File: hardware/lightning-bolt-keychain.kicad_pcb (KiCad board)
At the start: 2 copper layers, 70 x 114 mm, 9 parts, among them SW1 SPST

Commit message: Repair KiCad PCB and update parts notes
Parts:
- BT1: value CR2032 -> CR1220/CR1225
- SW1: footprint Button_Switch_SMD:SW_SPST_EVQP2 -> Button_Switch_SMD:SW_SPST_EVQP2_ShortPushTravel_H2.1mm
- moved D1 18.4 mm to (88.0, 52.0)
- moved R1 18.4 mm to (88.0, 58.0)
- moved D3 16.1 mm to (78.0, 92.0)
- moved R3 16.1 mm to (78.0, 98.0)
- moved SW1 6.00 mm to (80.0, 106.0)
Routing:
- net GND: track 54.8 -> 130.0 mm, vias 2 -> 1
- net +BATT: track 18.6 -> 55.4 mm
- net VLED: track 81.4 -> 65.4 mm
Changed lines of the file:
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@@
     (rev "A")
     (company "Open hardware concept")
-    (comment 1 "CR2032 amber LED keychain")
+    (comment 1 "12mm coin-cell amber LED keychain")
   )
   (layers
@@
   (footprint "Battery:BatteryHolder_Keystone_3000_1x12mm" (layer "B.Cu")
     (at 79 80 180)
-    (descr "CR2032 holder placeholder - verify exact ordered part")
+    (descr "12 mm coin-cell retainer - Keystone 3000 style")
     (property "Sheetfile" "lightning-bolt-keychain.kicad_sch")
     (property "Sheetname" "")
@@
       (effects (font (size 1 1) (thickness 0.15)) (justify mirror))
     )
-    (property "Value" "CR2032" (at 0 -13 180) (layer "B.Fab")
+    (property "Value" "CR1220/CR1225" (at 0 -13 180) (layer "B.Fab")
       (effects (font (size 1 1) (thickness 0.15)) (justify mirror))
     )
     (attr smd)
     (fp_circle (center 0 0) (end 11 0) (stroke (width 0.15) (type solid)) (fill none) (layer "B.SilkS"))
-    (pad "1" smd roundrect (at 0 -8 180) (size 5 3) (layers "B.Cu" "B.Paste" "B.Mask") (roundrect_rratio 0.2)
+    (pad "1" smd rect (at -7.9 0 180) (size 3.5 3.3) (layers "B.Cu" "B.Paste" "B.Mask")
       (net 2 "+BATT") (pinfunction "+") (pintype "passive"))
-    (pad "2" smd circle (at 0 0 180) (size 16 16) (layers "B.Cu" "B.Mask")
+    (pad "1" smd rect (at 7.9 0 180) (size 3.5 3.3) (layers "B.Cu" "B.Paste" "B.Mask")
+      (net 2 "+BATT") (pinfunction "+") (pintype "passive"))
+    (pad "2" smd circle (at 0 0 180) (size 10.2 10.2) (layers "B.Cu" "B.Mask")
       (net 1 "GND") (pinfunction "-") (pintype "passive"))
   )
-  (footprint "Button_Switch_SMD:SW_SPST_EVQP2" (layer "B.Cu")
-    (at 86 106 0)
+  (footprint "Button_Switch_SMD:SW_SPST_EVQP2_ShortPushTravel_H2.1mm" (layer "B.Cu")
+    (at 80 106 0)
     (property "Sheetfile" "lightning-bolt-keychain.kicad_sch")
     (property "Sheetname" "")
@@
   )
   (footprint "Resistor_SMD:R_0603_1608Metric" (layer "F.Cu")
-    (at 72 49 90)
+    (at 88 58 90)
     (property "Reference" "R1" (at -2 0 180) (layer "F.SilkS") (effects (font (size 0.8 0.8) (thickness 0.12))))
     (property "Value" "220" (at 0 1.6 90) (layer "F.Fab") (effects (font (size 0.8 0.8) (thickness 0.12))))
@@
   )
   (footprint "Resistor_SMD:R_0603_1608Metric" (layer "F.Cu")
-    (at 64 106 90)
+    (at 78 98 90)
     (property "Reference" "R3" (at -2 0 180) (layer "F.SilkS") (effects (font (size 0.8 0.8) (thickness 0.12))))
     (property "Value" "220" (at 0 1.6 90) (layer "F.Fab") (effects (font (size 0.8 0.8) (thickness 0.12))))
@@
   )
   (footprint "LED_SMD:LED_0603_1608Metric" (layer "F.Cu")
-    (at 72 43 90)
+    (at 88 52 90)
     (property "Reference" "D1" (at 2 0 180) (layer "F.SilkS") (effects (font (size 0.8 0.8) (thickness 0.12))))
     (property "Value" "Amber" (at 0 1.6 90) (layer "F.Fab") (effects (font (size 0.8 0.8) (thickness 0.12))))
@@
   )
   (footprint "LED_SMD:LED_0603_1608Metric" (layer "F.Cu")
-    (at 64 100 90)
+    (at 78 92 90)
     (property "Reference" "D3" (at 2 0 180) (layer "F.SilkS") (effects (font (size 0.8 0.8) (thickness 0.12))))
     (property "Value" "Amber" (at 0 1.6 90) (layer "F.Fab") (effects (font (size 0.8 0.8) (thickness 0.12))))
@@
     (property "Value" "Keyring_Hole" (at 0 6 0) (layer "F.Fab") hide (effects (font (size 1 1) (thickness 0.15))))
     (attr exclude_from_pos_files exclude_from_bom)
-    (fp_circle (center 0 0) (end 5.5 0) (stroke (width 0.2) (type solid)) (fill none) (layer "F.Cu"))
-    (fp_circle (center 0 0) (end 5.5 0) (stroke (width 0.2) (type solid)) (fill none) (layer "B.Cu"))
+    (fp_circle (center 0 0) (end 5.5 0) (stroke (width 0.2) (type solid)) (fill none) (layer "F.SilkS"))
+    (fp_circle (center 0 0) (end 5.5 0) (stroke (width 0.2) (type solid)) (fill none) (layer "B.SilkS"))
     (pad "1" thru_hole circle (at 0 0) (size 10 10) (drill 4.3) (layers "*.Cu" "*.Mask") (net 1 "GND"))
   )
-  ; Board outline: chunky manufacturable lightning bolt, roughly 70 mm x 115 mm.
   (gr_line (start 80 20) (end 110 20) (stroke (width 0.12) (type solid)) (layer "Edge.Cuts"))
   (gr_line (start 110 20) (end 116 62) (stroke (width 0.12) (type solid)) (layer "Edge.Cuts"))
@@
   (gr_line (start 58 44) (end 78 44) (stroke (width 0.12) (type solid)) (layer "Edge.Cuts"))
   (gr_line (start 78 44) (end 80 20) (stroke (width 0.12) (type solid)) (layer "Edge.Cuts"))
-  ; Front copper art traces, intended to show through ENIG on black solder mask.
   (gr_poly
     (pts
       (xy 66 40) (xy 68 40) (xy 74 68) (xy 72 68)
     )
-    (stroke (width 0.15) (type solid)) (fill solid) (layer "F.Cu"))
+    (stroke (width 0.15) (type solid)) (fill solid) (layer "F.SilkS"))
   (gr_poly
     (pts
       (xy 72 68) (xy 74 68) (xy 66 98) (xy 64 98)
     )
-    (stroke (width 0.15) (type solid)) (fill solid) (layer "F.Cu"))
-  (gr_line (start 83 26) (end 77 42) (stroke (width 0.6) (type solid)) (layer "F.Cu"))
-  (gr_line (start 97 42) (end 102 56) (stroke (width 0.45) (type solid)) (layer "F.Cu"))
-  (gr_line (start 57 62) (end 70 62) (stroke (width 0.45) (type solid)) (layer "F.Cu"))
-  (gr_line (start 89 73) (end 99 86) (stroke (width 0.45) (type solid)) (layer "F.Cu"))
-  (gr_line (start 62 111) (end 79 123) (stroke (width 0.45) (type solid)) (layer "F.Cu"))
-  (gr_circle (center 58 61) (end 59 61) (stroke (width 0.25) (type solid)) (fill solid) (layer "F.Cu"))
-  (gr_circle (center 101 52) (end 102 52) (stroke (width 0.25) (type solid)) (fill solid) (layer "F.Cu"))
-  (gr_circle (center 88 111) (end 89 111) (stroke (width 0.25) (type solid)) (fill solid) (layer "F.Cu"))
-  ; Functional routes.
-  (segment (start 88.25 106) (end 75 106.8) (width 0.3) (layer "F.Cu") (net 3))
-  (segment (start 75 106.8) (end 64 106.8) (width 0.3) (layer "F.Cu") (net 3))
-  (segment (start 75 106.8) (end 75 77.8) (width 0.3) (layer "F.Cu") (net 3))
-  (segment (start 75 77.8) (end 72 49.8) (width 0.3) (layer "F.Cu") (net 3))
-  (segment (start 72 48.2) (end 72 43.8) (width 0.3) (layer "F.Cu") (net 4))
+    (stroke (width 0.15) (type solid)) (fill solid) (layer "F.SilkS"))
+  (gr_line (start 83 26) (end 77 42) (stroke (width 0.6) (type solid)) (layer "F.SilkS"))
+  (gr_line (start 97 42) (end 102 56) (stroke (width 0.45) (type solid)) (layer "F.SilkS"))
+  (gr_line (start 57 62) (end 70 62) (stroke (width 0.45) (type solid)) (layer "F.SilkS"))
+  (gr_line (start 89 73) (end 99 86) (stroke (width 0.45) (type solid)) (layer "F.SilkS"))
+  (gr_line (start 62 111) (end 79 123) (stroke (width 0.45) (type solid)) (layer "F.SilkS"))
+  (gr_circle (center 58 61) (end 59 61) (stroke (width 0.25) (type solid)) (fill solid) (layer "F.SilkS"))
+  (gr_circle (center 101 52) (end 102 52) (stroke (width 0.25) (type solid)) (fill solid) (layer "F.SilkS"))
+  (gr_circle (center 88 111) (end 89 111) (stroke (width 0.25) (type solid)) (fill solid) (layer "F.SilkS"))
+  (segment (start 86.9 80) (end 77.75 106) (width 0.4) (layer "B.Cu") (net 2))
+  (segment (start 71.1 80) (end 71.1 74) (width 0.4) (layer "B.Cu") (net 2))
+  (segment (start 71.1 74) (end 86.9 74) (width 0.4) (layer "B.Cu") (net 2))
+  (segment (start 86.9 74) (end 86.9 80) (width 0.4) (layer "B.Cu") (net 2))
+  (segment (start 94 29) (end 94 51.2) (width 0.3) (layer "F.Cu") (net 1))
+  (segment (start 94 51.2) (end 72 51.2) (width 0.3) (layer "F.Cu") (net 1))
+  (via (at 82.25 106) (size 0.8) (drill 0.4) (layers "F.Cu" "B.Cu") (net 3))
+  (via (at 79 80) (size 0.8) (drill 0.4) (layers "F.Cu" "B.Cu") (net 1))
+  (segment (start 82.25 106) (end 78 98.8) (width 0.3) (layer "F.Cu") (net 3))
+  (segment (start 78 98.8) (end 82 98.8) (width 0.3) (layer "F.Cu") (net 3))
+  (segment (start 82 98.8) (end 82 77.8) (width 0.3) (layer "F.Cu") (net 3))
+  (segment (start 82 77.8) (end 75 77.8) (width 0.3) (layer "F.Cu") (net 3))
+  (segment (start 82 77.8) (end 88 77.8) (width 0.3) (layer "F.Cu") (net 3))
+  (segment (start 88 77.8) (end 88 58.8) (width 0.3) (layer "F.Cu") (net 3))
+  (segment (start 88 57.2) (end 88 52.8) (width 0.3) (layer "F.Cu") (net 4))
   (segment (start 75 76.2) (end 75 71.8) (width 0.3) (layer "F.Cu") (net 5))
-  (segment (start 64 105.2) (end 64 100.8) (width 0.3) (layer "F.Cu") (net 6))
-  (segment (start 72 42.2) (end 86 35) (width 0.3) (layer "F.Cu") (net 1))
-  (segment (start 75 70.2) (end 86 80) (width 0.3) (layer "F.Cu") (net 1))
-  (segment (start 64 99.2) (end 79 80) (width 0.3) (layer "F.Cu") (net 1))
-  (segment (start 83.75 106) (end 79 88) (width 0.4) (layer "B.Cu") (net 2))
-  (via (at 88.25 106) (size 0.8) (drill 0.4) (layers "F.Cu" "B.Cu") (net 3))
-  (via (at 86 35) (size 0.8) (drill 0.4) (layers "F.Cu" "B.Cu") (net 1))
-  (via (at 86 80) (size 0.8) (drill 0.4) (layers "F.Cu" "B.Cu") (net 1))
-  (zone (net 1) (net_name "GND") (layer "B.Cu") (hatch edge 0.5)
+  (segment (start 78 97.2) (end 78 92.8) (width 0.3) (layer "F.Cu") (net 6))
+  (segment (start 88 51.2) (end 72 51.2) (width 0.3) (layer "F.Cu") (net 1))
+  (segment (start 72 51.2) (end 72 80) (width 0.3) (layer "F.Cu") (net 1))
+  (segment (start 72 80) (end 79 80) (width 0.3) (layer "F.Cu") (net 1))
+  (segment (start 75 70.2) (end 73 70.2) (width 0.3) (layer "F.Cu") (net 1))
+  (segment (start 73 70.2) (end 73 80) (width 0.3) (layer "F.Cu") (net 1))
+  (segment (start 73 80) (end 79 80) (width 0.3) (layer "F.Cu") (net 1))
+  (segment (start 78 91.2) (end 73 91.2) (width 0.3) (layer "F.Cu") (net 1))
+  (segment (start 73 91.2) (end 73 80) (width 0.3) (layer "F.Cu") (net 1))
+(zone (net 1) (net_name "GND") (layer "B.Cu") (hatch edge 0.5)
     (connect_pads (clearance 0.25))
     (min_thickness 0.25) (filled_areas_thickness no)

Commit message: Clean up KiCad schematic and PCB visuals
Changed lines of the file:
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@@
   (gr_line (start 58 44) (end 78 44) (stroke (width 0.12) (type solid)) (layer "Edge.Cuts"))
   (gr_line (start 78 44) (end 80 20) (stroke (width 0.12) (type solid)) (layer "Edge.Cuts"))
-  (gr_poly
-    (pts
-      (xy 66 40) (xy 68 40) (xy 74 68) (xy 72 68)
-    )
-    (stroke (width 0.15) (type solid)) (fill solid) (layer "F.SilkS"))
-  (gr_poly
-    (pts
-      (xy 72 68) (xy 74 68) (xy 66 98) (xy 64 98)
-    )
-    (stroke (width 0.15) (type solid)) (fill solid) (layer "F.SilkS"))
-  (gr_line (start 83 26) (end 77 42) (stroke (width 0.6) (type solid)) (layer "F.SilkS"))
-  (gr_line (start 97 42) (end 102 56) (stroke (width 0.45) (type solid)) (layer "F.SilkS"))
-  (gr_line (start 57 62) (end 70 62) (stroke (width 0.45) (type solid)) (layer "F.SilkS"))
-  (gr_line (start 89 73) (end 99 86) (stroke (width 0.45) (type solid)) (layer "F.SilkS"))
-  (gr_line (start 62 111) (end 79 123) (stroke (width 0.45) (type solid)) (layer "F.SilkS"))
-  (gr_circle (center 58 61) (end 59 61) (stroke (width 0.25) (type solid)) (fill solid) (layer "F.SilkS"))
-  (gr_circle (center 101 52) (end 102 52) (stroke (width 0.25) (type solid)) (fill solid) (layer "F.SilkS"))
-  (gr_circle (center 88 111) (end 89 111) (stroke (width 0.25) (type solid)) (fill solid) (layer "F.SilkS"))
   (segment (start 86.9 80) (end 77.75 106) (width 0.4) (layer "B.Cu") (net 2))
   (segment (start 71.1 80) (end 71.1 74) (width 0.4) (layer "B.Cu") (net 2))

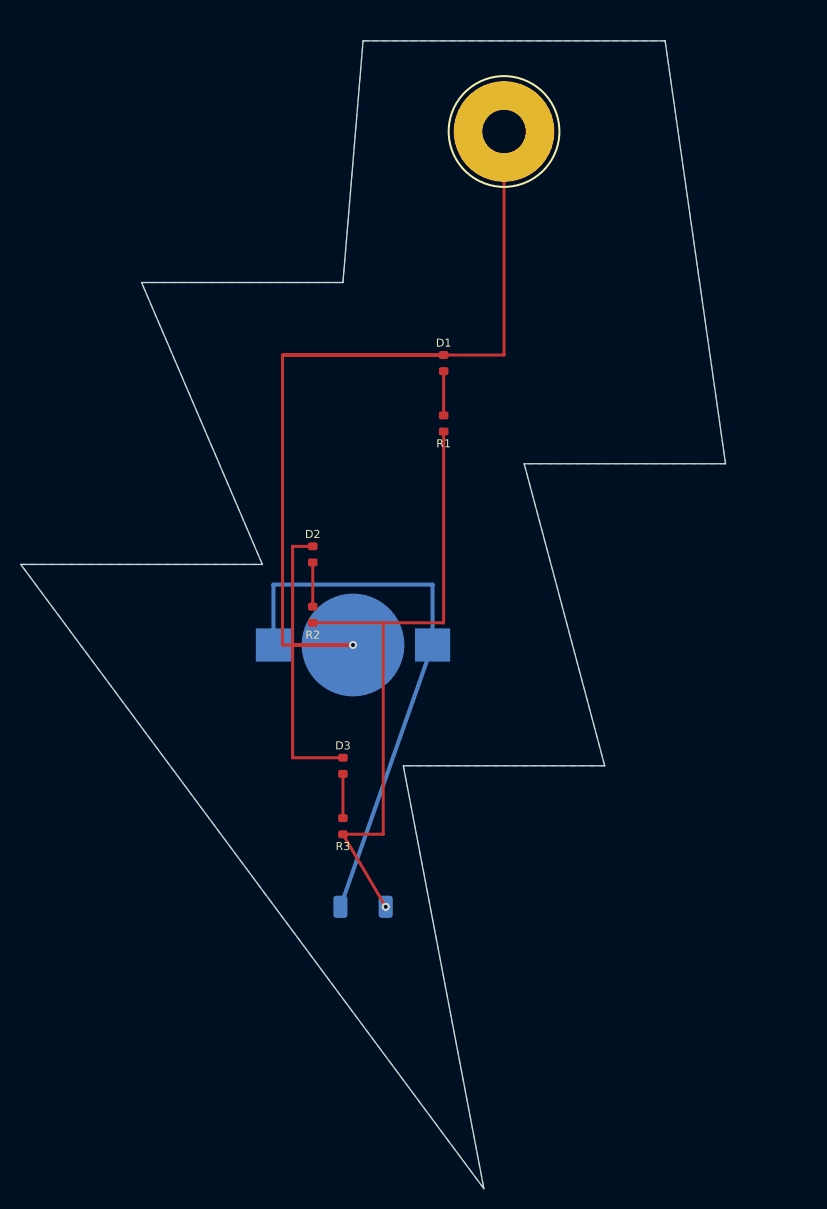
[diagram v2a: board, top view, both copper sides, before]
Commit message: Convert keychain to USB-C powered design
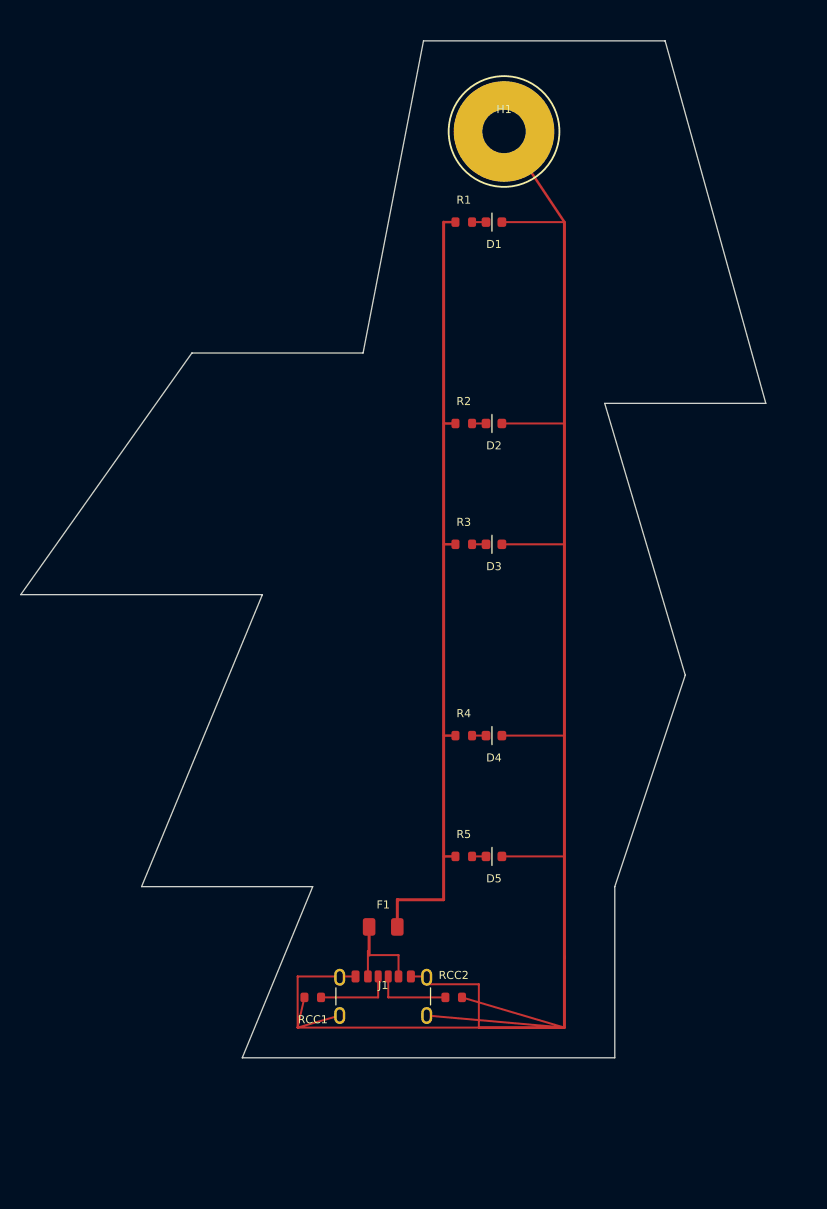
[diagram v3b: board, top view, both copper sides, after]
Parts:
- removed BT1: CR1220/CR1225, Battery:BatteryHolder_Keystone_3000_1x12mm
- removed SW1: SPST, Button_Switch_SMD:SW_SPST_EVQP2_ShortPushTravel_H2.1mm
- added D4: Amber, LED_SMD:LED_0603_1608Metric, F.Cu at (93.0, 89.0)
- added D5: Amber, LED_SMD:LED_0603_1608Metric, F.Cu at (93.0, 101.0)
- added F1: 500mA, Fuse:Fuse_1206_3216Metric, F.Cu at (82.0, 108.0)
- added J1: USB-C Power, Connector_USB:USB_C_Receptacle_GCT_USB4125-xx-x_6P_TopMnt_Horizontal, F.Cu at (82.0, 116.0)
- added R4: 1k, Resistor_SMD:R_0603_1608Metric, F.Cu at (90.0, 89.0)
- added R5: 1k, Resistor_SMD:R_0603_1608Metric, F.Cu at (90.0, 101.0)
- added RCC1: 5.1k, Resistor_SMD:R_0603_1608Metric, F.Cu at (75.0, 115.0)
- added RCC2: 5.1k, Resistor_SMD:R_0603_1608Metric, F.Cu at (89.0, 115.0)
- H1: value Keyring_Hole -> Keyring
- R1, R2, R3: value 220 -> 1k
- moved R3 30.5 mm to (90.0, 70.0), turned to 0 degrees
- moved D3 26.6 mm to (93.0, 70.0), turned to 180 degrees
- moved R2 24.2 mm to (90.0, 58.0), turned to 0 degrees
- moved D2 22.2 mm to (93.0, 58.0), turned to 180 degrees
- moved R1 20.1 mm to (90.0, 38.0), turned to 0 degrees
- moved D1 14.9 mm to (93.0, 38.0), turned to 180 degrees
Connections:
- D1 pad 1: LED1 -> GND
- D1 pad 2: GND -> LED1
- D2 pad 1: LED2 -> GND
- D2 pad 2: GND -> LED2
- D3 pad 1: LED3 -> GND
- D3 pad 2: GND -> LED3
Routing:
- net GND: track 130.0 -> 211.6 mm, vias 1 -> 0
- net +BATT: track 55.4 -> 0.00 mm
- net VLED: track 65.4 -> 80.5 mm, vias 1 -> 0
- net VBUS: track 0.00 -> 10.5 mm
- net CC2: track 0.00 -> 7.75 mm
- net CC1: track 0.00 -> 7.75 mm
- net LED3: track 4.40 -> 1.39 mm
- net LED2: track 4.40 -> 1.39 mm
- net LED1: track 4.40 -> 1.39 mm
- net LED5: track 0.00 -> 1.39 mm
- net LED4: track 0.00 -> 1.39 mm
- removed copper zone on B.Cu, net GND
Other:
- board size 70 x 114 mm -> 74 x 101 mm
